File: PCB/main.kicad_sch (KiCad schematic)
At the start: 2 parts

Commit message: Develop schematic a little and create initial software project
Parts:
- added C1, C2: ${Capacitance}, Capacitor_SMD:C_0402_1005Metric, symbol 0 LibDB:Capacitors/CMP-0005
- added U1, U2: MCP2558FD, Package_SO:SOIC-8_3.9x4.9mm_P1.27mm, symbol 0 LibDB:ICs/CMP-0002
- added U3: STM32G0B1, Package_QFP:LQFP-48_7x7mm_P0.5mm, symbol 0 LibDB:ICs/CMP-0003
- added Y1: ${Frequency}, Crystal:Crystal_SMD_2016-4Pin_2.0x1.6mm, symbol 0 LibDB:Crystals/CMP-0004
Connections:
- new net: C1.2, U3.8 (PF0), Y1.1
- new net: C2.2, U3.10 (PF2), Y1.3
- new net Earth: C1.1, C2.1, U3.7 (VSS), Y1.2, Y1.4

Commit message: Develop board
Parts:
- removed R1, R2: 120R, symbol Device:R_Small
- added C3, C4, C6: ${Capacitance}, Capacitor_SMD:C_0603_1608Metric, symbol 0 LibDB:Capacitors/CMP-0008
- added C5: ${Capacitance}, Capacitor_SMD:C_0805_2012Metric, symbol 0 LibDB:Capacitors/CMP-0009
- added R1, R2: ${Resistance}, Resistor_SMD:R_1206_3216Metric, symbol 0 LibDB:Resistors/CMP-0006
- added R10, R9: ${Resistance}, Resistor_SMD:R_0402_1005Metric, symbol 0 LibDB:Resistors/CMP-0010
- added R3, R4, R5, R6, R7, R8: ${Resistance}, Resistor_SMD:R_0402_1005Metric, symbol 0 LibDB:Resistors/CMP-0007
- added SW1: SPST, libdb:CMP-0011, symbol 0 LibDB:Switches/CMP-0011
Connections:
- net Earth: now also U1.2 (VSS), U2.2 (VSS), C3.1, C4.1, C5.1, C6.2, R10.2, R9.2, SW1.1
- net FDCAN1_TX: now reaches U1.1 (TXD)
- net FDCAN1_TX: now also R3.1
- net at U1.4 (RXD): now also R4.1
- net at U1.6 (CANL): now also R1.1, R2.1
- net at U1.7 (CANH): now also R1.2, R2.2
- net FDCAN1_S: now reaches U1.8 (S)
- net FDCAN1_S: now also R8.1, R9.1
- net at C2.2, Y1.3: now also U3.9 (PF1); no longer U3.10 (PF2)
- net FDCAN2_TX: now reaches U2.1 (TXD)
- net FDCAN2_TX: now also R6.2
- net at U2.4 (RXD): now also R5.1
- net FDCAN2_S: now reaches U2.8 (S)
- net FDCAN2_S: now also R10.1, R7.2
- net FDCAN2_RX: now reaches U3.19 (PB0)
- net FDCAN2_RX: now also R5.2
- net at U3.20 (PB1): now also R6.1
- net at U3.22 (PB10): now also R7.1
- net SWDIO: now reaches U3.35 (PA13)
- net SWDCLK: now reaches U3.36 (PA14)
- net FDCAN1_RX: now reaches U3.38 (PD0)
- net FDCAN1_RX: now also R4.2
- net at U3.39 (PD1): now also R3.2
- net at U3.4 (VBAT): now also U3.6 (VDD), C3.2, C5.2
- net at U3.41 (PD3): now also R8.2
- net at U3.5 (VREF+): now also C4.2
- new net: C6.1, SW1.2, U3.10 (PF2)
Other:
- moved on the sheet: C1, C2, U1, U2, U3, Y1

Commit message: Further develop board
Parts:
- added C10, C9: ${Capacitance}, Capacitor_Tantalum_SMD:CP_EIA-3528-15_AVX-H, symbol 0 LibDB:Capacitors/CMP-0017
- added C11, C12: ${Capacitance}, Capacitor_SMD:C_0805_2012Metric, symbol 0 LibDB:Capacitors/CMP-0020
- added C13, C14, C15, C6: ${Capacitance}, Capacitor_SMD:C_0402_1005Metric, symbol 0 LibDB:Capacitors/CMP-0021
- added C8: ${Capacitance}, Capacitor_SMD:CP_Elec_10x10, symbol 0 LibDB:Capacitors/CMP-0018
- added D1: SS36, Diode_SMD:D_SMC, symbol 0 LibDB:Schottky Diodes/CMP-0016
- added D3: LED_B, Device:LED_Small, symbol 0 LibDB:LEDs/CMP-0023
- added J1, J2: S20B-PADSS-1, libdb:CMP-0012, symbol 0 LibDB:Connectors/CMP-0012
- added J4: SWD, libdb:CMP-0022, symbol 0 LibDB:Connectors/CMP-0022
- added L1: ${Inductance}, Inductor_SMD:L_1210_3225Metric, symbol 0 LibDB:Inductors/CMP-0015
- added R11: ${Resistance}, Resistor_SMD:R_0402_1005Metric, symbol 0 LibDB:Resistors/CMP-0024
- added U4: LM2596-5.0, Package_TO_SOT_SMD:TO-263-5_TabPin3, symbol 0 LibDB:DC-DC Converters/CMP-0014
- added U5: XC6206P33, libdb:CMP-0019, symbol 0 LibDB:LDO Regulators/CMP-0019
- C1: renamed from C4; Voltage Rating 50 V -> 50V
- C3: Voltage Rating 50 V -> 50V
- C4: renamed from C1; Voltage Rating 50 V -> 50V
- C5: renamed from C2; Voltage Rating 50 V -> 50V
- C7: renamed from C6; Voltage Rating 50 V -> 50V
- U1: Manufacturer Microchip Technology -> Microchip Technology
- U3: renamed from U2; Manufacturer Microchip Technology -> Microchip Technology
- Y1: footprint Crystal:Crystal_SMD_2016-4Pin_2.0x1.6mm -> libdb:CMP-0004
- renumbered C5 to C2, R7 to R10, R4 to R2, R2 to R3, R9 to R4, R3 to R5, R8 to R6, R5 to R7, R6 to R8, R10 to R9, U3 to U2
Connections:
- net Earth: now also C2.2, C3.2, C10.2, C11.2, C12.2, C13.2, C14.2, C15.2, C6.2, C8.2, C9.2, D1.2 (A), D3.1 (K), J1.9 (Pin_9), J2.2 (Pin_2), J4.3 (GND), U4.3 (GND), U4.5 (~{ON}/OFF), U5.1 (GND); no longer C2.1, C3.1
- net SWDCLK: now also J4.2 (SWDCLK)
- net SWDIO: now also J4.4 (SWDIO)
- net +5V: now reaches U1.3 (VDD)
- net +5V: now also U3.3 (VDD), C10.1, C11.1, C14.1, C15.1, C9.1, L1.2, U4.4 (FB), U5.3 (VI)
- net +3.3V: now reaches U1.5 (VIO)
- net +3.3V: now also C2.1, C3.1, U2.4 (VBAT), U2.6 (VDD), U3.5 (VIO), C12.1, C13.1, C6.1, J4.1 (+3.3V), U5.2 (VO)
- net at U2.12 (PA1): now also R11.1
- new net: D1.1 (K), L1.1, U4.2 (OUT)
- new net: D3.2 (A), R11.2
- new net +BATT: C8.1, J1.10 (Pin_10), J2.1 (Pin_1), U4.1 (VIN)
- new net JST_01_AUX_IN: J1.1 (Pin_1), J2.10 (Pin_10)
- new net JST_02_AUX_IN: J1.2 (Pin_2), J2.9 (Pin_9)
- new net JST_03_AUX_IN: J1.3 (Pin_3), J2.8 (Pin_8)
- new net JST_04_NC: J1.4 (Pin_4), J2.7 (Pin_7)
- new net JST_05_BK_VID_IN: J1.5 (Pin_5), J2.6 (Pin_6)
- new net JST_06_CAN: J1.6 (Pin_6), J2.5 (Pin_5)
- new net JST_07_CAN: J1.7 (Pin_7), J2.4 (Pin_4)
- new net JST_08_CAM_DET: J1.8 (Pin_8), J2.3 (Pin_3)
- new net JST_11_AUDIO_FL: J1.11 (Pin_11), J2.20 (Pin_20)
- new net JST_12_AUDIO_FL: J1.12 (Pin_12), J2.19 (Pin_19)
- new net JST_13_AUDIO_FL: J1.13 (Pin_13), J2.18 (Pin_18)
- new net JST_14_AUDIO_FL: J1.14 (Pin_14), J2.17 (Pin_17)
- new net JST_15_VID_IN: J1.15 (Pin_15), J2.16 (Pin_16)
- new net JST_16_NC: J1.16 (Pin_16), J2.15 (Pin_15)
- new net JST_17_CAN: J1.17 (Pin_17), J2.14 (Pin_14)
- new net JST_18_CAN: J1.18 (Pin_18), J2.13 (Pin_13)
- new net JST_19_CAM_12V+: J1.19 (Pin_19), J2.12 (Pin_12)
- new net JST_20_NC: J1.20 (Pin_20), J2.11 (Pin_11)
- no-connect marks 0 -> 32
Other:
- moved on the sheet: C1, C2, C3, C4, C5, C7, R1, R10, R2, R3, R4, R5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

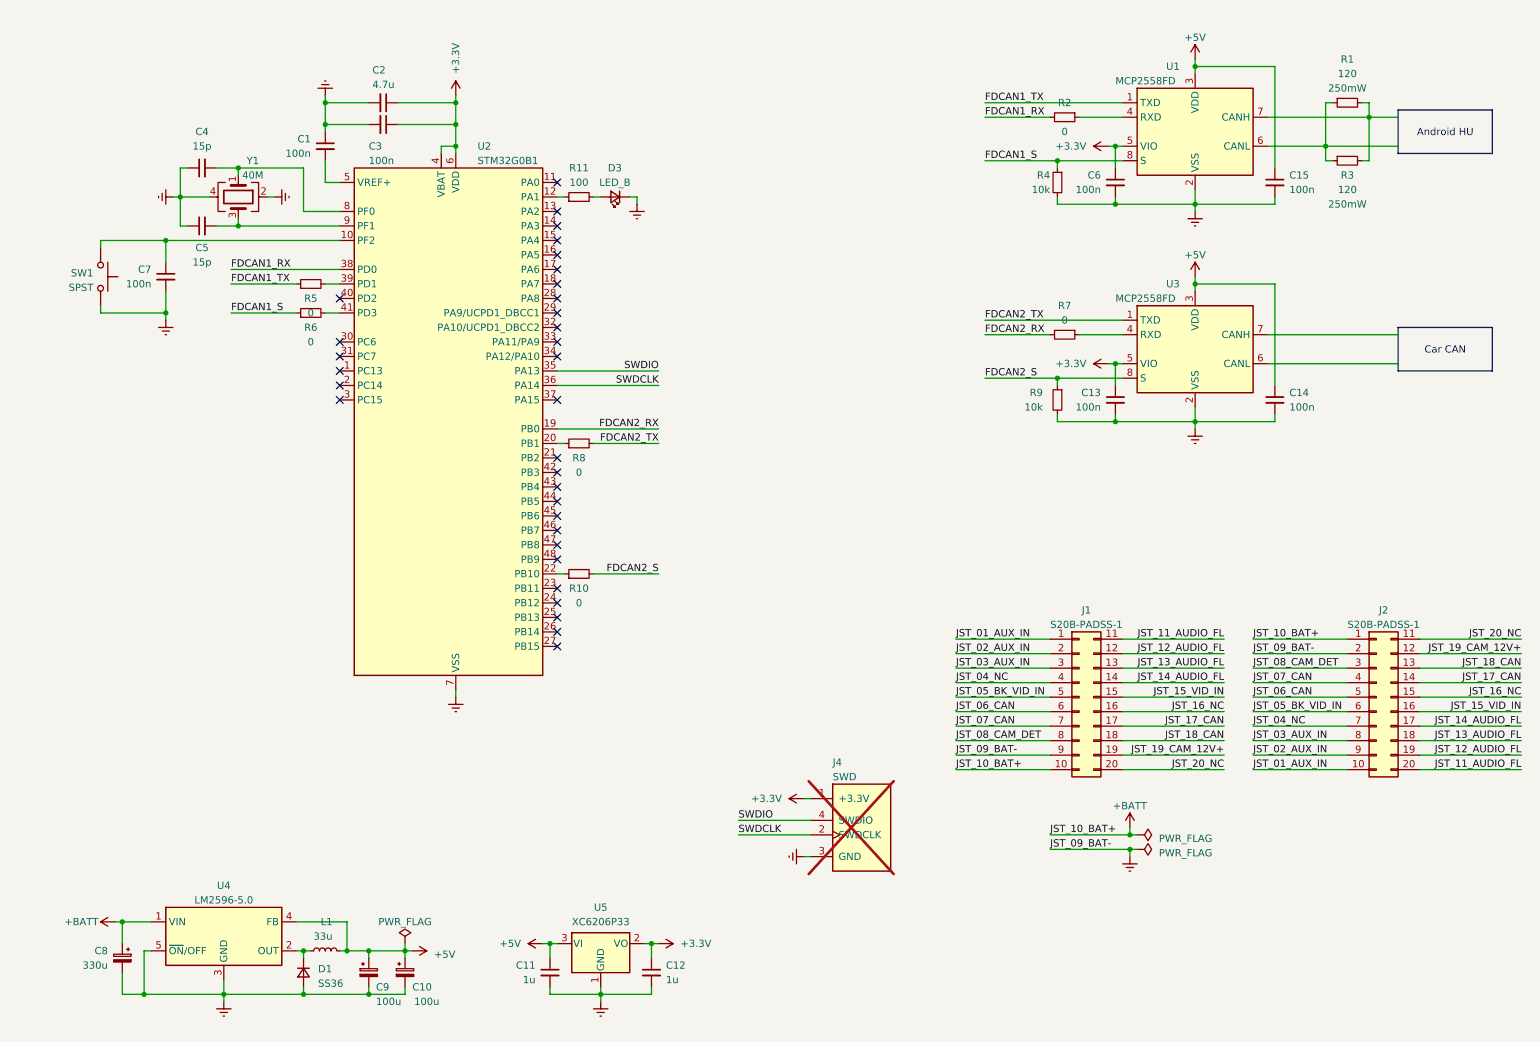
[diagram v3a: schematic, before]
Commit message: Finish schematic
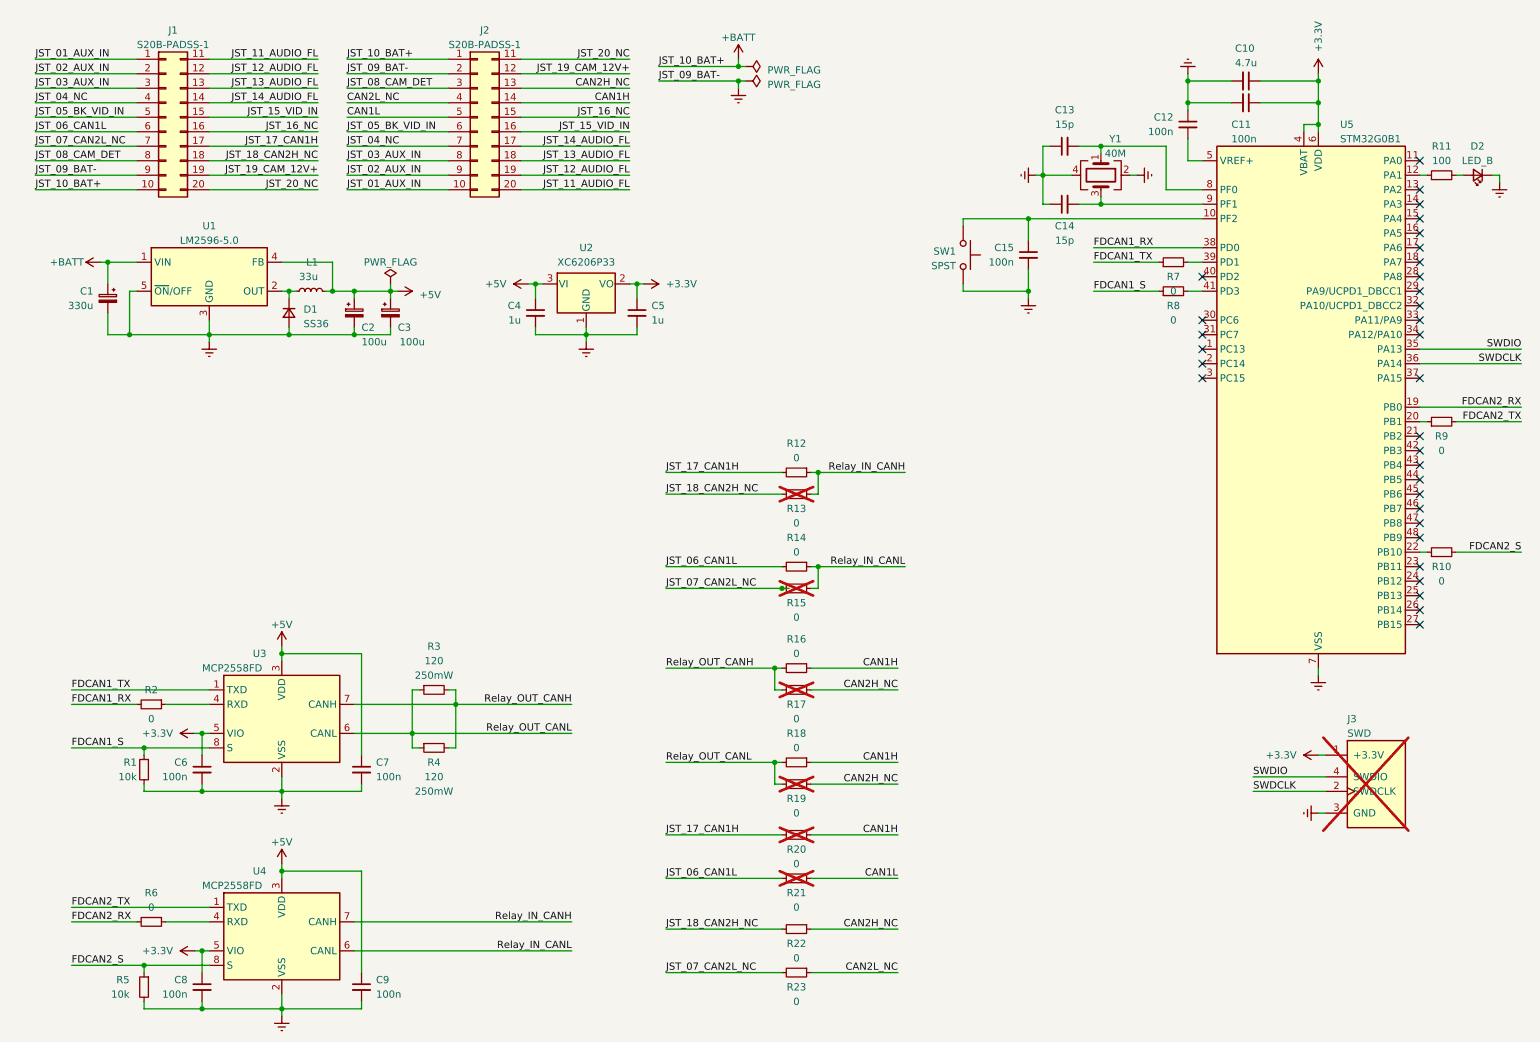
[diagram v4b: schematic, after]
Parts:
- added R12, R13, R14, R15, R16, R17, R18, R19, R20, R21, R22, R23: ${Resistance}, Resistor_SMD:R_0402_1005Metric, symbol 0 LibDB:Resistors/CMP-0007
- renumbered C8 to C1, C2 to C10, C3 to C11, C1 to C12, C4 to C13, C5 to C14, C7 to C15, C9 to C2, C10 to C3, C11 to C4, C12 to C5, C15 to C7, C13 to C8, C14 to C9, D3 to D2, J4 to J3, R4 to R1, R1 to R3, R3 to R4, R9 to R5, R7 to R6, R5 to R7, R6 to R8, R8 to R9, U4 to U1, U5 to U2, U1 to U3, U3 to U4, U2 to U5
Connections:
- net Relay_OUT_CANL: now reaches R3.1, R4.1, U3.6 (CANL)
- net Relay_OUT_CANL: now also R18.2, R19.2
- net Relay_OUT_CANH: now reaches R3.2, R4.2, U3.7 (CANH)
- net Relay_OUT_CANH: now also R16.2, R17.2
- net Relay_IN_CANL: now reaches U4.6 (CANL)
- net Relay_IN_CANL: now also R14.1, R15.1
- net Relay_IN_CANH: now reaches U4.7 (CANH)
- net Relay_IN_CANH: now also R12.1, R13.1
- net JST_06_CAN renamed CAN1L
- net CAN1L: now also R21.1; no longer J1.6 (Pin_6)
- net JST_07_CAN renamed CAN2L_NC
- net CAN2L_NC: now also R23.1; no longer J1.7 (Pin_7)
- net JST_17_CAN renamed CAN1H
- net CAN1H: now also R16.1, R18.1, R20.1; no longer J1.17 (Pin_17)
- net JST_18_CAN renamed CAN2H_NC
- net CAN2H_NC: now also R17.1, R19.1, R22.1; no longer J1.18 (Pin_18)
- new net JST_06_CAN1L: J1.6 (Pin_6), R14.2, R21.2
- new net JST_07_CAN2L_NC: J1.7 (Pin_7), R15.2, R23.2
- new net JST_17_CAN1H: J1.17 (Pin_17), R12.2, R20.2
- new net JST_18_CAN2H_NC: J1.18 (Pin_18), R13.2, R22.2
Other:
- title: (none) -> BMW F20 AHU CAN Relay
- moved on the sheet: C1, C10, C11, C12, C13, C14, C15, C2, C3, C4, C5, C6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

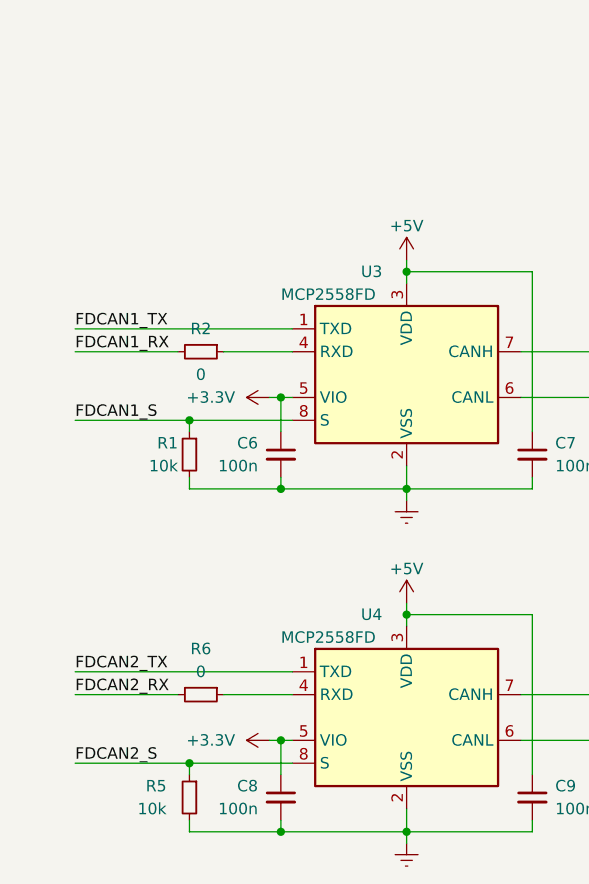
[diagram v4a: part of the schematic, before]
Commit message: Switch Silent mode on by default
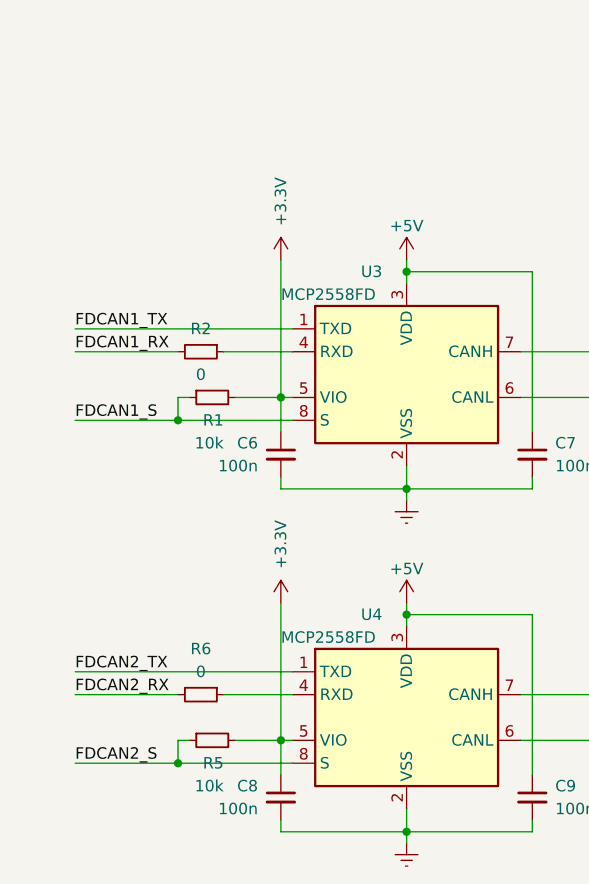
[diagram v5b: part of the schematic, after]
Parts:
- D2: footprint Device:LED_Small -> LED_SMD:LED_0402_1005Metric
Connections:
- net +3.3V: now also R1.2, R5.2
- net Earth: no longer R1.2, R5.2
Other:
- moved on the sheet: R1, R5
